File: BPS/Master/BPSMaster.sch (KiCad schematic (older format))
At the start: 21 parts, among them J1 SWD, J13 CAN Analyzer, J5 SPI Analyzer, SW1 B3SL-1002P, U1 STM32F413RHTx, Y1 8M

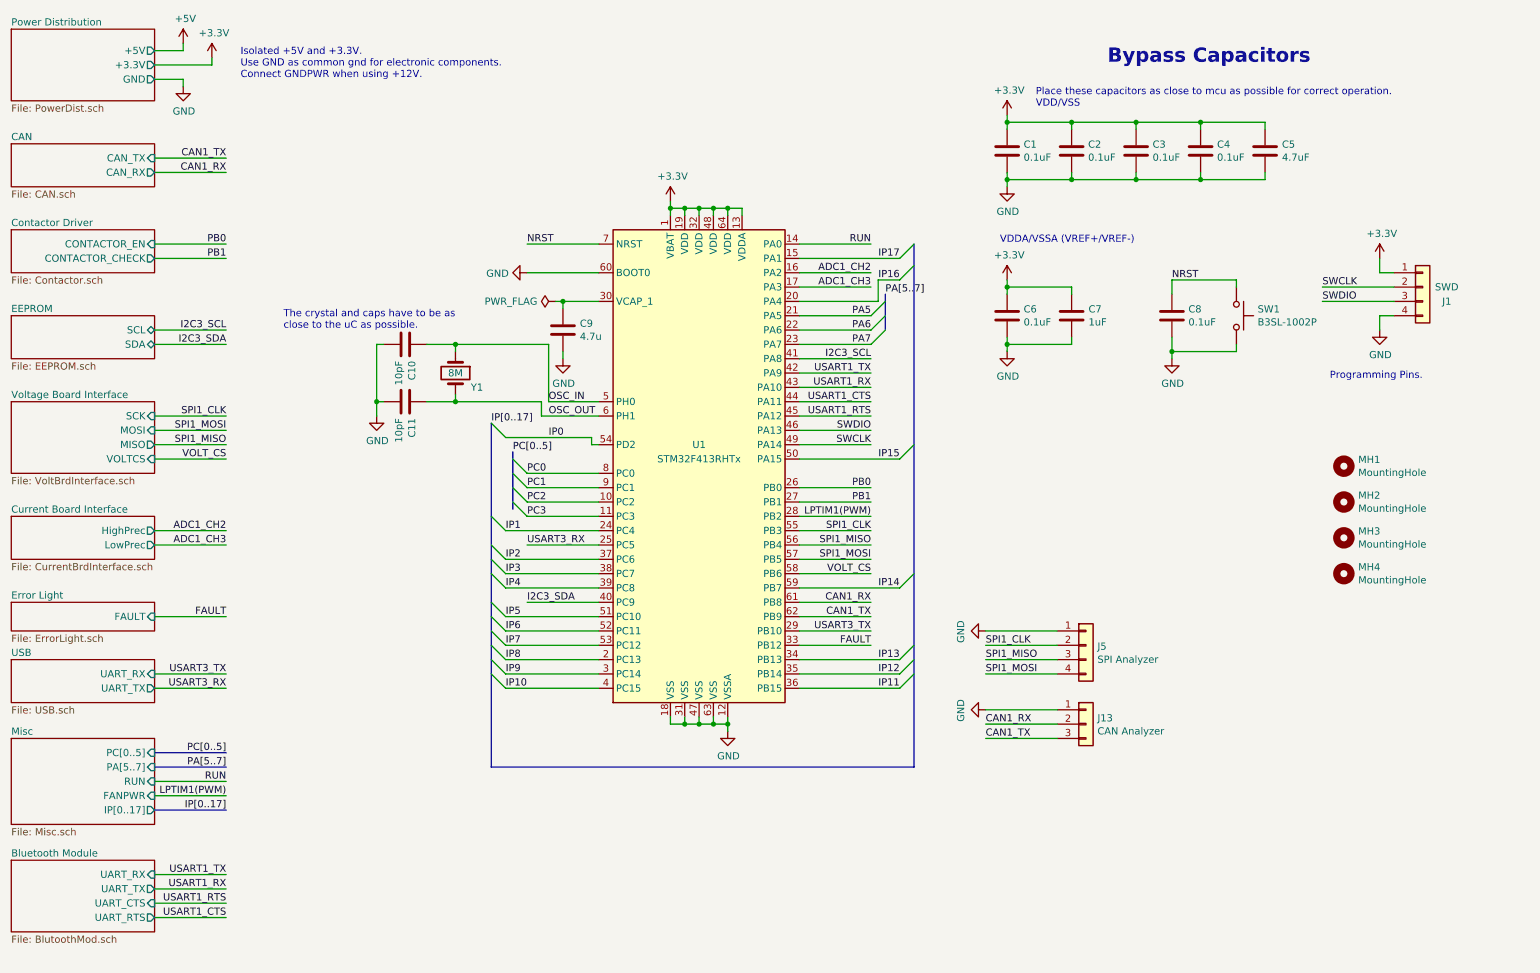
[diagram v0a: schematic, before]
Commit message: Created new board for Bluetooth module because the antenna cannot have a ground plane on it. Made everything connect using pin headers. Will mount the Bluetooth module board onto the Master board.
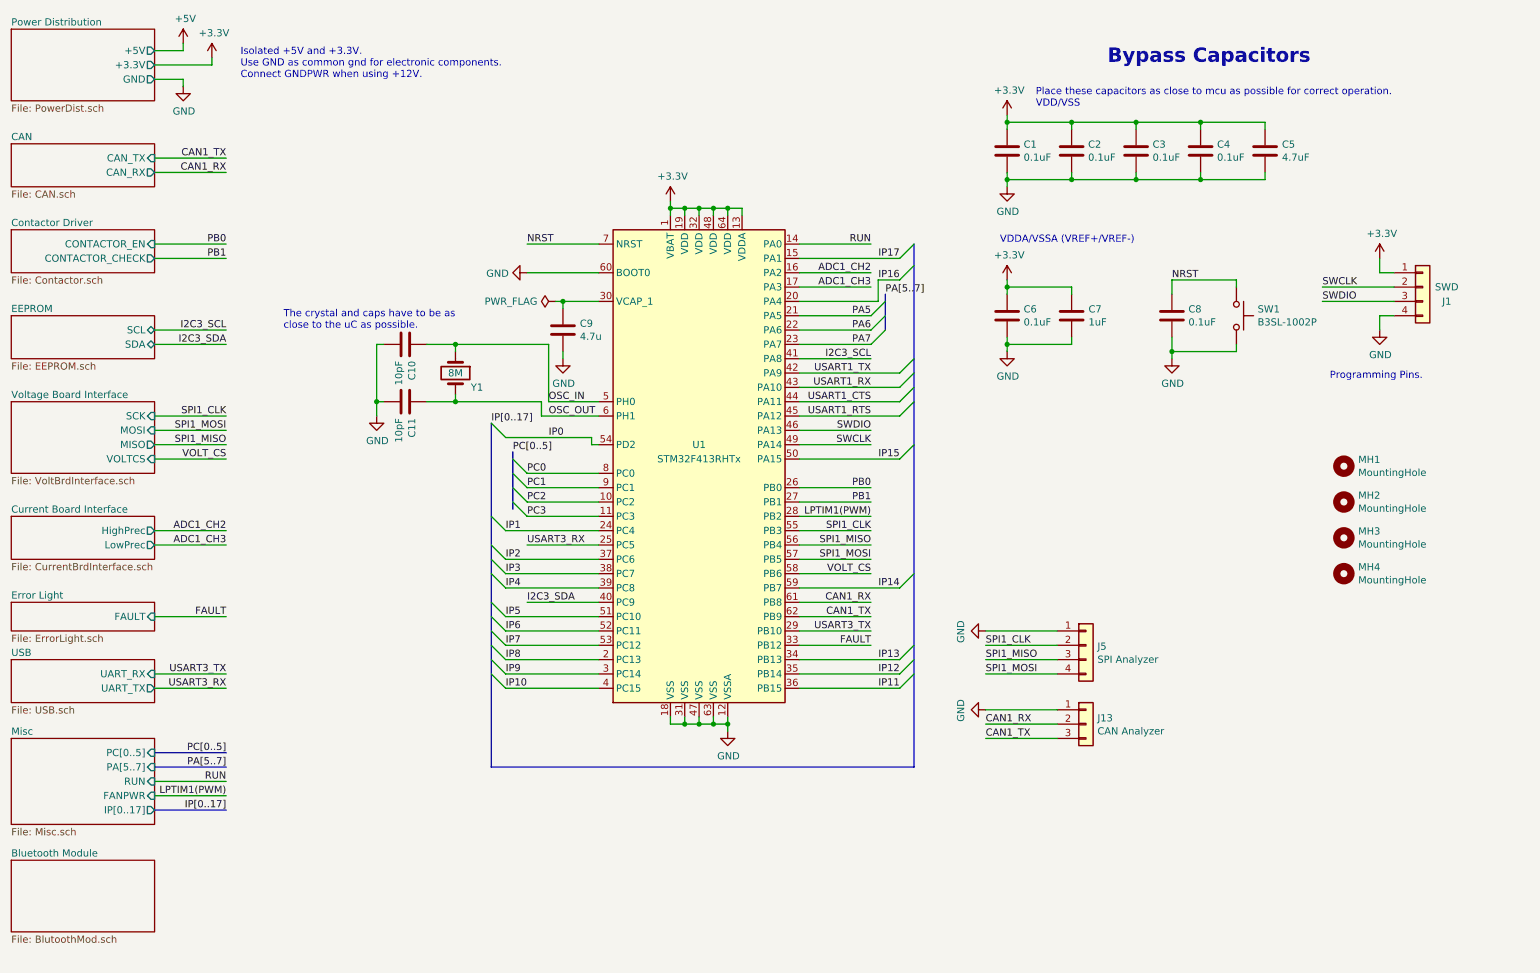
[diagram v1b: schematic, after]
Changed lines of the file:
@@
 Text Label 7800 5400 0    50   ~ 0
 SPI1_MOSI
-Text Label 2500 6900 2    50   ~ 0
-USART1_RX
-Text Label 2500 6800 2    50   ~ 0
-USART1_TX
 Text Label 7000 4300 2    50   ~ 0
 LPTIM1(PWM)
@@
 Text Label 7000 3600 2    50   ~ 0
 USART1_RTS
-Text Label 2500 7000 2    50   ~ 0
-USART1_RTS
-Text Label 2500 7100 2    50   ~ 0
-USART1_CTS
 $Comp
 L MCU_ST_STM32F4:STM32F413RHTx U1
@@
 F0 "Bluetooth Module" 50
 F1 "BlutoothMod.sch" 50
-F2 "UART_RX" I R 2000 6800 50
-F3 "UART_TX" O R 2000 6900 50
-F4 "UART_CTS" I R 2000 7000 50
-F5 "UART_RTS" O R 2000 7100 50
 $EndSheet
 Text Label 4450 4400 0    50   ~ 0
@@
 	6500 3900 7200 3900
 Wire Wire Line
-	2000 7100 2500 7100
-Wire Wire Line
-	2000 7000 2500 7000
-Wire Wire Line
-	6500 3600 7000 3600
-Wire Wire Line
-	6500 3500 7000 3500
-Wire Wire Line
-	6500 3400 7000 3400
-Wire Wire Line
-	6500 3300 7000 3300
-Wire Wire Line
 	2000 6250 2500 6250
 Wire Wire Line
 	6500 4300 7000 4300
-Wire Wire Line
-	2000 6800 2500 6800
-Wire Wire Line
-	2000 6900 2500 6900
 Wire Wire Line
 	8300 5400 7800 5400
@@
 Wire Wire Line
 	4750 3100 4750 3500
+Entry Wire Line
+	7200 3300 7300 3200
+Entry Wire Line
+	7200 3400 7300 3300
+Entry Wire Line
+	7200 3500 7300 3400
+Entry Wire Line
+	7200 3600 7300 3500
+Wire Wire Line
+	6500 3300 7200 3300
+Wire Wire Line
+	6500 3400 7200 3400
+Wire Wire Line
+	6500 3500 7200 3500
+Wire Wire Line
+	6500 3600 7200 3600
 Wire Bus Line
 	7100 2750 7100 3000
@@
 	4500 3850 4500 4250
 Wire Bus Line
+	4350 3650 4350 6050
+Wire Bus Line
 	7300 2400 7300 6050
-Wire Bus Line
-	4350 3650 4350 6050
 $EndSCHEMATC

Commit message: Finished adding interface pins to master board. For some reason, the mosfet track isn't letting me connect to the fan power. I'm not sure why all these schematics are listed as modified because I didn't change anything in them.
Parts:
- added J16: Conn_01x06, Connector_PinHeader_2.54mm:PinHeader_1x06_P2.54mm_Vertical, symbol Connector_Generic:Conn_01x06
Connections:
- wire segments 165 -> 179
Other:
- note added: "Bluetooth\nModule\nConnections"
- moved on the sheet: C6, C7, C8, SW1
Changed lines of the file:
@@
 $Descr A4 11693 8268
 encoding utf-8
-Sheet 1 11
+Sheet 1 10
 Title ""
 Date ""
@@
 L power:+3.3V #PWR09
 U 1 1 5C25EB0C
-P 7950 2650
-F 0 "#PWR09" H 7950 2500 50  0001 C CNN
-F 1 "+3.3V" H 7965 2823 50  0000 C CNN
-F 2 "" H 7950 2650 50  0001 C CNN
-F 3 "" H 7950 2650 50  0001 C CNN
-	1    7950 2650
+P 8550 2650
+F 0 "#PWR09" H 8550 2500 50  0001 C CNN
+F 1 "+3.3V" H 8565 2823 50  0000 C CNN
+F 2 "" H 8550 2650 50  0001 C CNN
+F 3 "" H 8550 2650 50  0001 C CNN
+	1    8550 2650
 	1    0    0    -1
 $EndComp
@@
 L Device:C C6
 U 1 1 5C25EB12
-P 7950 2900
-F 0 "C6" H 8065 2946 50  0000 L CNN
-F 1 "0.1uF" H 8065 2855 50  0000 L CNN
-F 2 "Capacitor_SMD:C_0805_2012Metric" H 7988 2750 50  0001 C CNN
-F 3 "~" H 7950 2900 50  0001 C CNN
-	1    7950 2900
-	1    0    0    -1
-$EndComp
-Text Notes 7900 2400 0    50   ~ 0
+P 8550 2900
+F 0 "C6" H 8665 2946 50  0000 L CNN
+F 1 "0.1uF" H 8665 2855 50  0000 L CNN
+F 2 "Capacitor_SMD:C_0805_2012Metric" H 8588 2750 50  0001 C CNN
+F 3 "~" H 8550 2900 50  0001 C CNN
+	1    8550 2900
+	1    0    0    -1
+$EndComp
+Text Notes 8500 2400 0    50   ~ 0
 VDDA/VSSA (VREF+/VREF-)
 $Comp
 L power:GND #PWR011
 U 1 1 5C25EB2D
-P 7950 3150
-F 0 "#PWR011" H 7950 2900 50  0001 C CNN
-F 1 "GND" H 7955 2977 50  0000 C CNN
-F 2 "" H 7950 3150 50  0001 C CNN
-F 3 "" H 7950 3150 50  0001 C CNN
-	1    7950 3150
+P 8550 3150
+F 0 "#PWR011" H 8550 2900 50  0001 C CNN
+F 1 "GND" H 8555 2977 50  0000 C CNN
+F 2 "" H 8550 3150 50  0001 C CNN
+F 3 "" H 8550 3150 50  0001 C CNN
+	1    8550 3150
 	1    0    0    -1
 $EndComp
@@
 L Device:C C7
 U 1 1 5C25F2B0
-P 8400 2900
-F 0 "C7" H 8518 2946 50  0000 L CNN
-F 1 "1uF" H 8518 2855 50  0000 L CNN
-F 2 "Capacitor_SMD:C_0805_2012Metric" H 8438 2750 50  0001 C CNN
-F 3 "~" H 8400 2900 50  0001 C CNN
-	1    8400 2900
+P 9000 2900
+F 0 "C7" H 9118 2946 50  0000 L CNN
+F 1 "1uF" H 9118 2855 50  0000 L CNN
+F 2 "Capacitor_SMD:C_0805_2012Metric" H 9038 2750 50  0001 C CNN
+F 3 "~" H 9000 2900 50  0001 C CNN
+	1    9000 2900
 	1    0    0    -1
 $EndComp
@@
 L Device:C C8
 U 1 1 5C32FFDF
-P 9100 2900
-F 0 "C8" H 9215 2946 50  0000 L CNN
-F 1 "0.1uF" H 9215 2855 50  0000 L CNN
-F 2 "Capacitor_SMD:C_0805_2012Metric" H 9138 2750 50  0001 C CNN
-F 3 "~" H 9100 2900 50  0001 C CNN
-	1    9100 2900
+P 9350 2900
+F 0 "C8" H 9465 2946 50  0000 L CNN
+F 1 "0.1uF" H 9465 2855 50  0000 L CNN
+F 2 "Capacitor_SMD:C_0805_2012Metric" H 9388 2750 50  0001 C CNN
+F 3 "~" H 9350 2900 50  0001 C CNN
+	1    9350 2900
 	1    0    0    -1
 $EndComp
@@
 L power:GND #PWR013
 U 1 1 5C336510
-P 9100 3200
-F 0 "#PWR013" H 9100 2950 50  0001 C CNN
-F 1 "GND" H 9105 3027 50  0000 C CNN
-F 2 "" H 9100 3200 50  0001 C CNN
-F 3 "" H 9100 3200 50  0001 C CNN
-	1    9100 3200
+P 9350 3200
+F 0 "#PWR013" H 9350 2950 50  0001 C CNN
+F 1 "GND" H 9355 3027 50  0000 C CNN
+F 2 "" H 9350 3200 50  0001 C CNN
+F 3 "" H 9350 3200 50  0001 C CNN
+	1    9350 3200
 	1    0    0    -1
 $EndComp
@@
 L Switch:SW_Push SW1
 U 1 1 5C339C0A
-P 9550 2900
-F 0 "SW1" V 9504 3048 50  0000 L CNN
-F 1 "B3SL-1002P" V 9595 3048 50  0000 L CNN
-F 2 "Button_Switch_SMD:SW_SPST_B3SL-1002P" H 9550 3100 50  0001 C CNN
-F 3 "" H 9550 3100 50  0001 C CNN
-	1    9550 2900
+P 9800 2900
+F 0 "SW1" V 9754 3048 50  0000 L CNN
+F 1 "B3SL-1002P" V 9845 3048 50  0000 L CNN
+F 2 "Button_Switch_SMD:SW_SPST_B3SL-1002P" H 9800 3100 50  0001 C CNN
+F 3 "" H 9800 3100 50  0001 C CNN
+	1    9800 2900
 	0    1    1    0
 $EndComp
 Text Label 4600 2400 0    50   ~ 0
 NRST
-Text Label 9100 2650 0    50   ~ 0
+Text Label 9350 2650 0    50   ~ 0
 NRST
 $Sheet
@@
 Text Label 4500 3850 0    50   ~ 0
 PC[0..5]
-$Sheet
-S 1000 6700 1000 500
-U 5EE39517
-F0 "Bluetooth Module" 50
-F1 "BlutoothMod.sch" 50
-$EndSheet
 Text Label 4450 4400 0    50   ~ 0
 IP1
@@
 	5100 2400 4600 2400
 Wire Wire Line
-	9550 3100 9550 3150
-Wire Wire Line
-	9550 2650 9550 2700
-Wire Wire Line
-	9100 2650 9100 2750
-Wire Wire Line
-	9100 3050 9100 3150
-Connection ~ 9100 3150
-Wire Wire Line
-	9100 3200 9100 3150
-Wire Wire Line
-	9100 3150 9550 3150
-Wire Wire Line
-	9100 2650 9550 2650
+	9800 3100 9800 3150
+Wire Wire Line
+	9800 2650 9800 2700
+Wire Wire Line
+	9350 2650 9350 2750
+Wire Wire Line
+	9350 3050 9350 3150
+Connection ~ 9350 3150
+Wire Wire Line
+	9350 3200 9350 3150
+Wire Wire Line
+	9350 3150 9800 3150
+Wire Wire Line
+	9350 2650 9800 2650
 Wire Wire Line
 	2000 1150 2400 1150
@@
 Wire Wire Line
 	6000 5800 6000 5750
-Connection ~ 7950 3100
-Wire Wire Line
-	7950 3150 7950 3100
-Wire Wire Line
-	8400 3050 8400 3100
-Wire Wire Line
-	7950 3100 8400 3100
-Wire Wire Line
-	7950 3050 7950 3100
-Wire Wire Line
-	8400 2750 8400 2700
-Wire Wire Line
-	7950 2700 7950 2750
-Connection ~ 7950 2700
-Wire Wire Line
-	7950 2700 8400 2700
-Wire Wire Line
-	7950 2650 7950 2700
+Connection ~ 8550 3100
+Wire Wire Line
+	8550 3150 8550 3100
+Wire Wire Line
+	9000 3050 9000 3100
+Wire Wire Line
+	8550 3100 9000 3100
+Wire Wire Line
+	8550 3050 8550 3100
+Wire Wire Line
+	9000 2750 9000 2700
+Wire Wire Line
+	8550 2700 8550 2750
+Connection ~ 8550 2700
+Wire Wire Line
+	8550 2700 9000 2700
+Wire Wire Line
+	8550 2650 8550 2700
 Connection ~ 7950 1950
 Wire Wire Line
@@
 Entry Wire Line
 	4450 5500 4350 5400
-Text Label 4350 3650 0    50   ~ 0
-IP[0..17]
 Wire Bus Line
 	2000 6350 2500 6350
@@
 Wire Wire Line
 	4750 3100 4750 3500
-Entry Wire Line
-	7200 3300 7300 3200
-Entry Wire Line
-	7200 3400 7300 3300
-Entry Wire Line
-	7200 3500 7300 3400
-Entry Wire Line
-	7200 3600 7300 3500
-Wire Wire Line
-	6500 3300 7200 3300
-Wire Wire Line
-	6500 3400 7200 3400
-Wire Wire Line
-	6500 3500 7200 3500
-Wire Wire Line
-	6500 3600 7200 3600
+Text Label 4350 3650 0    50   ~ 0
+IP[0..17]
+$Comp
+L Connector_Generic:Conn_01x06 J?
+U 1 1 5F08CE6F
+P 7700 3500
+AR Path="/5C392C6A/5F08CE6F" Ref="J?"  Part="1"
+AR Path="/5F08CE6F" Ref="J16"  Part="1"
+F 0 "J16" V 7900 3350 50  0000 L CNN
+F 1 "Conn_01x06" V 7800 3200 50  0000 L CNN
+F 2 "Connector_PinHeader_2.54mm:PinHeader_1x06_P2.54mm_Vertical" H 7700 3500 50  0001 C CNN
+F 3 "~" H 7700 3500 50  0001 C CNN
+	1    7700 3500
+	1    0    0    1
+$EndComp
+Wire Wire Line
+	7500 3700 7450 3700
+Wire Wire Line
+	7450 3700 7450 3750
+Wire Wire Line
+	7500 3200 7450 3200
+Wire Wire Line
+	7450 3200 7450 3150
+$Comp
+L power:GND #PWR?
+U 1 1 5F08CE79
+P 7450 3750
+AR Path="/5C392C6A/5F08CE79" Ref="#PWR?"  Part="1"
+AR Path="/5F08CE79" Ref="#PWR033"  Part="1"
+F 0 "#PWR033" H 7450 3500 50  0001 C CNN
+F 1 "GND" V 7350 3700 50  0000 R CNN
+F 2 "" H 7450 3750 50  0001 C CNN
+F 3 "" H 7450 3750 50  0001 C CNN
+	1    7450 3750
+	-1   0    0    -1
+$EndComp
+$Comp
+L power:+3.3V #PWR?
+U 1 1 5F08CE7F
+P 7450 3150
+AR Path="/5C392C6A/5F08CE7F" Ref="#PWR?"  Part="1"
+AR Path="/5F08CE7F" Ref="#PWR028"  Part="1"
+F 0 "#PWR028" H 7450 3000 50  0001 C CNN
+F 1 "+3.3V" V 7350 3300 50  0000 C CNN
+F 2 "" H 7450 3150 50  0001 C CNN
+F 3 "" H 7450 3150 50  0001 C CNN
+	1    7450 3150
+	-1   0    0    -1
+$EndComp
+Wire Wire Line
+	7400 3300 7400 3400
+Wire Wire Line
+	7400 3400 7500 3400
+Wire Wire Line
+	6500 3300 7400 3300
+Wire Wire Line
+	6500 3400 7350 3400
+Wire Wire Line
+	7350 3400 7350 3350
+Wire Wire Line
+	7350 3350 7500 3350
+Wire Wire Line
+	7500 3350 7500 3300
+Wire Wire Line
+	6500 3500 7400 3500
+Wire Wire Line
+	7400 3500 7400 3600
+Wire Wire Line
+	7400 3600 7500 3600
+Wire Wire Line
+	6500 3600 7350 3600
+Wire Wire Line
+	7350 3600 7350 3550
+Wire Wire Line
+	7350 3550 7500 3550
+Wire Wire Line
+	7500 3550 7500 3500
+Text Notes 7600 4000 0    50   ~ 0
+Bluetooth\nModule\nConnections
 Wire Bus Line
 	7100 2750 7100 3000
@@
 	4500 3850 4500 4250
 Wire Bus Line
-	4350 3650 4350 6050
+	7300 2350 7300 6050
 Wire Bus Line
-	7300 2400 7300 6050
+	4350 3600 4350 6050
 $EndSCHEMATC

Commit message: Reverts edited files that are not related to the FanBoard back to master branch's versions
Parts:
- removed J16: Conn_01x06, Connector_PinHeader_2.54mm:PinHeader_1x06_P2.54mm_Vertical, symbol Connector_Generic:Conn_01x06
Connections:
- net labels removed: IP0, IP1, IP10, IP11, IP12, IP13, IP14, IP15, IP16, IP17, IP2, IP3, IP4, IP5, IP6, IP7, IP8, IP9, IP[0..17], LPTIM1(PWM), USART1_CTS, USART1_RTS, USART1_RX, USART1_TX
- wire segments 179 -> 137
- no-connect marks 0 -> 23
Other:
- note removed: "Bluetooth\nModule\nConnections"
- moved on the sheet: C10, C11, C6, C7, C8, SW1, Y1

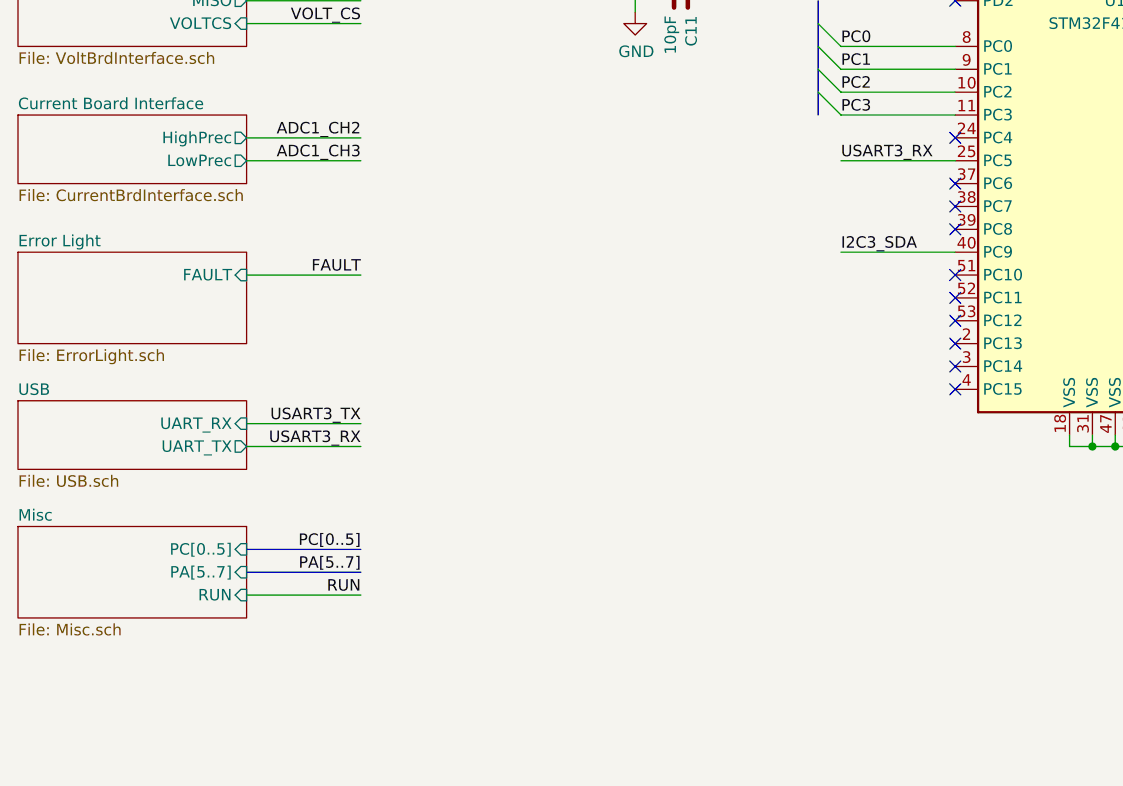
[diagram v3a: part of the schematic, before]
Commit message: Created new sheet for bluetooth module. Using pins 37 and 38 of STM for UART communication with module. May need others to configure bluetooth module for low power mode.
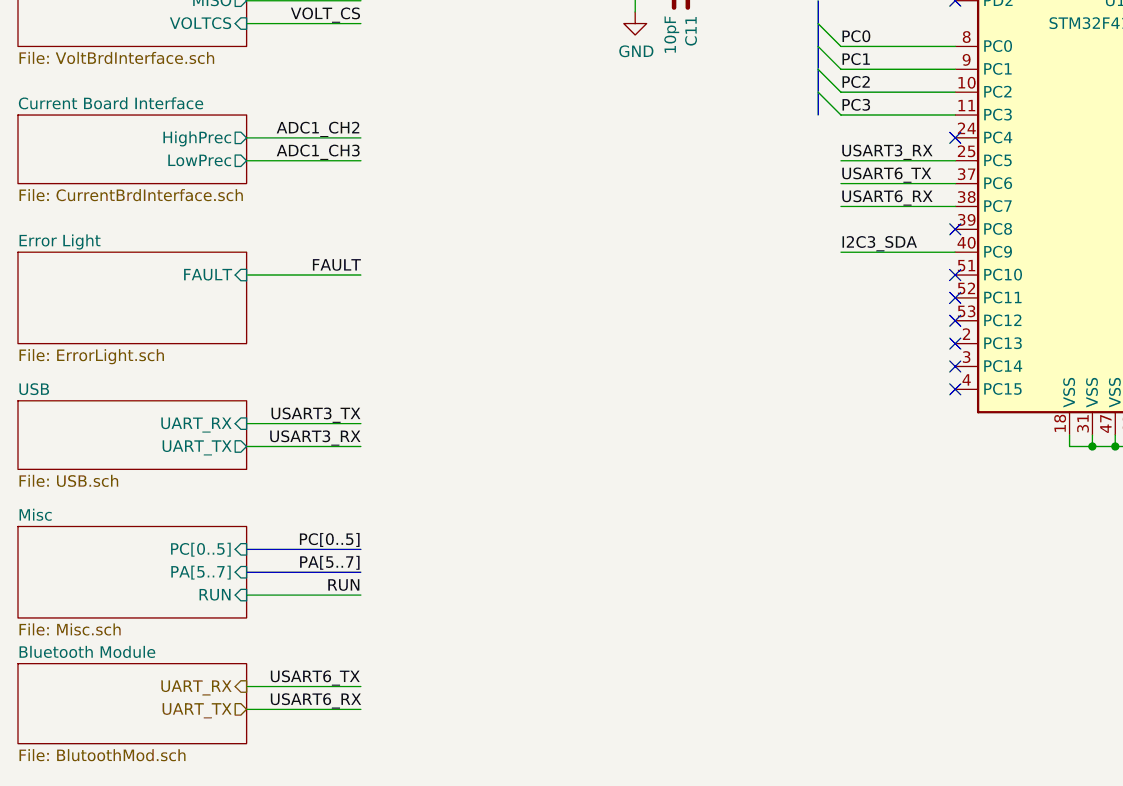
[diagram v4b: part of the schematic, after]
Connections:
- net UART_RX: now reaches U1.37 (PC6)
- net UART_TX: now reaches U1.38 (PC7)
- no-connect marks 23 -> 21
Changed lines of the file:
@@
 $Descr A4 11693 8268
 encoding utf-8
-Sheet 1 10
+Sheet 1 11
 Title ""
 Date ""
@@
 Text Label 7800 5850 0    50   ~ 0
 CAN1_TX
-NoConn ~ 5100 4600
-NoConn ~ 5100 4700
 NoConn ~ 5100 4800
 NoConn ~ 6500 5300
@@
 Text Label 7800 5400 0    50   ~ 0
 SPI1_MOSI
+Wire Wire Line
+	5100 4600 4600 4600
+Wire Wire Line
+	5100 4700 4600 4700
+Text Label 4600 4600 0    50   ~ 0
+USART6_TX
+Text Label 4600 4700 0    50   ~ 0
+USART6_RX
+$Sheet
+S 1000 6700 1000 350
+U 5EE39517
+F0 "Bluetooth Module" 50
+F1 "BlutoothMod.sch" 50
+$EndSheet
+Text HLabel 2000 6800 0    50   Output ~ 0
+UART_RX
+Text HLabel 2000 6900 0    50   Input ~ 0
+UART_TX
+Wire Wire Line
+	2000 6800 2500 6800
+Wire Wire Line
+	2000 6900 2500 6900
 Wire Bus Line
 	7100 2700 7100 3000
 Wire Bus Line
 	4500 3800 4500 4300
+Text Label 2100 6800 0    50   ~ 0
+USART6_TX
+Text Label 2100 6900 0    50   ~ 0
+USART6_RX
 $EndSCHEMATC
